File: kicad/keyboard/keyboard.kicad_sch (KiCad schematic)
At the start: 119 parts, among them SW1 SW_MX, SW10 SW_MX, SW11 SW_MX, SW12 SW_MX, SW13 SW_MX, SW14 SW_MX, SW15 SW_MX, SW16 SW_MX, SW17 SW_MX, SW18 SW_MX, SW19 SW_MX, SW2 SW_MX, SW20 SW_MX, SW21 SW_MX, SW22 SW_MX, SW23 SW_MX, SW24 SW_MX, SW25 SW_MX, SW26 SW_MX, SW27 SW_MX, SW28 SW_MX, SW29 SW_MX, SW3 SW_MX, SW30 SW_MX, SW31 SW_MX, SW32 SW_MX, SW33 SW_MX, SW34 SW_MX, SW35 SW_MX, SW36 SW_MX, SW37 SW_MX, SW38 SW_MX, SW39 SW_MX, SW4 SW_MX, SW40 SW_MX, SW41 SW_MX, SW42 SW_MX, SW43 SW_MX, SW44 SW_MX, SW45 SW_MX, SW46 SW_MX, SW47 SW_MX, SW48 SW_MX, SW49 SW_MX, SW5 SW_MX, SW50 SW_MX, SW51 SW_MX, SW52 SW_MX, SW53 SW_MX, SW54 SW_MX, SW55 SW_MX, SW56 SW_MX, SW57 SW_MX, SW58 SW_MX, SW59 SW_MX, SW6 SW_MX, SW7 SW_MX, SW8 SW_MX, SW9 SW_MX

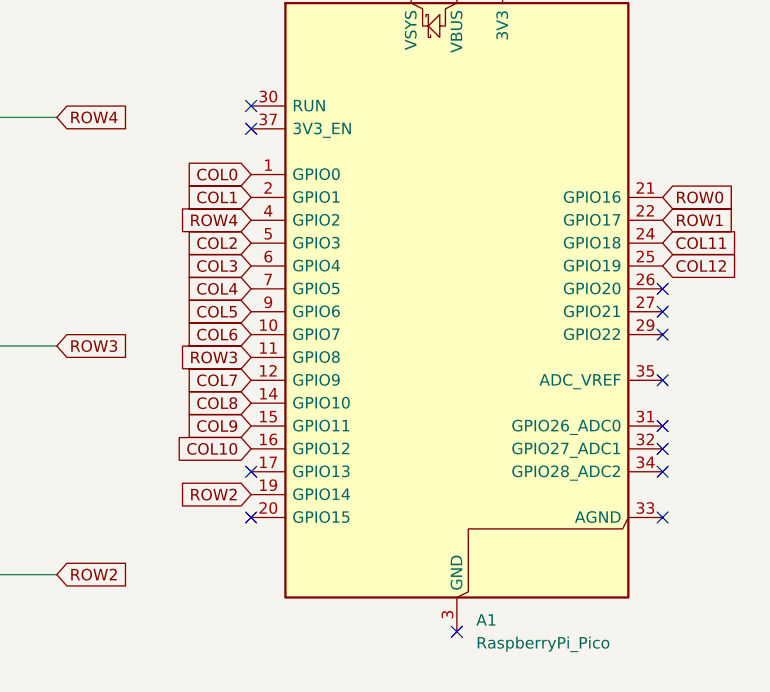
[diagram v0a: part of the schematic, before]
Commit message: Connect rows and columns to Pico
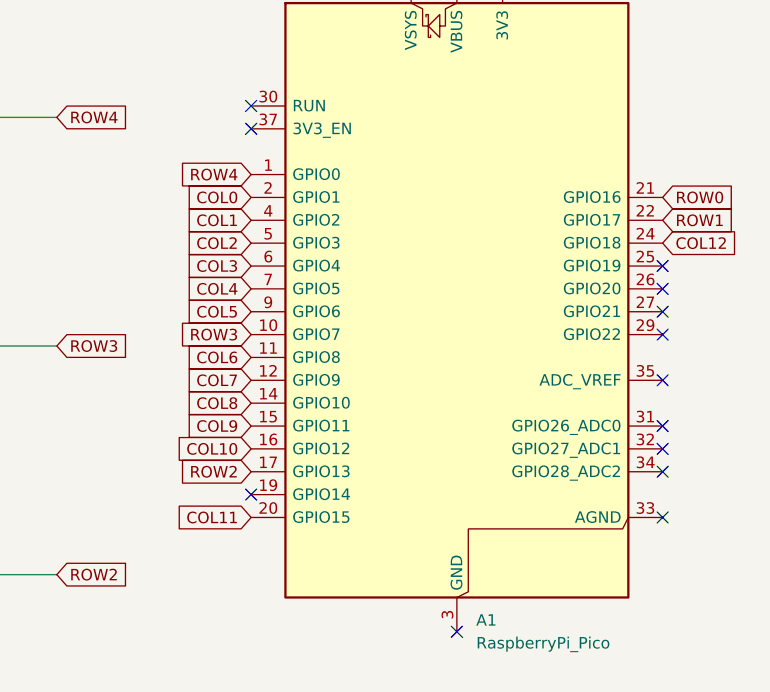
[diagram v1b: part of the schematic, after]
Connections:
- net COL0: now also A1.2 (GPIO1); no longer A1.1 (GPIO0)
- net COL1: now also A1.4 (GPIO2); no longer A1.2 (GPIO1)
- net COL11: now also A1.20 (GPIO15); no longer A1.24 (GPIO18)
- net COL12: now also A1.24 (GPIO18); no longer A1.25 (GPIO19)
- net COL6: now also A1.11 (GPIO8); no longer A1.10 (GPIO7)
- net ROW2: now also A1.17 (GPIO13); no longer A1.19 (GPIO14)
- net ROW3: now also A1.10 (GPIO7); no longer A1.11 (GPIO8)
- net ROW4: now also A1.1 (GPIO0); no longer A1.4 (GPIO2)
